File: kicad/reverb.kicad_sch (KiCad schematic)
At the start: 17 parts, among them IC1 TL072CP

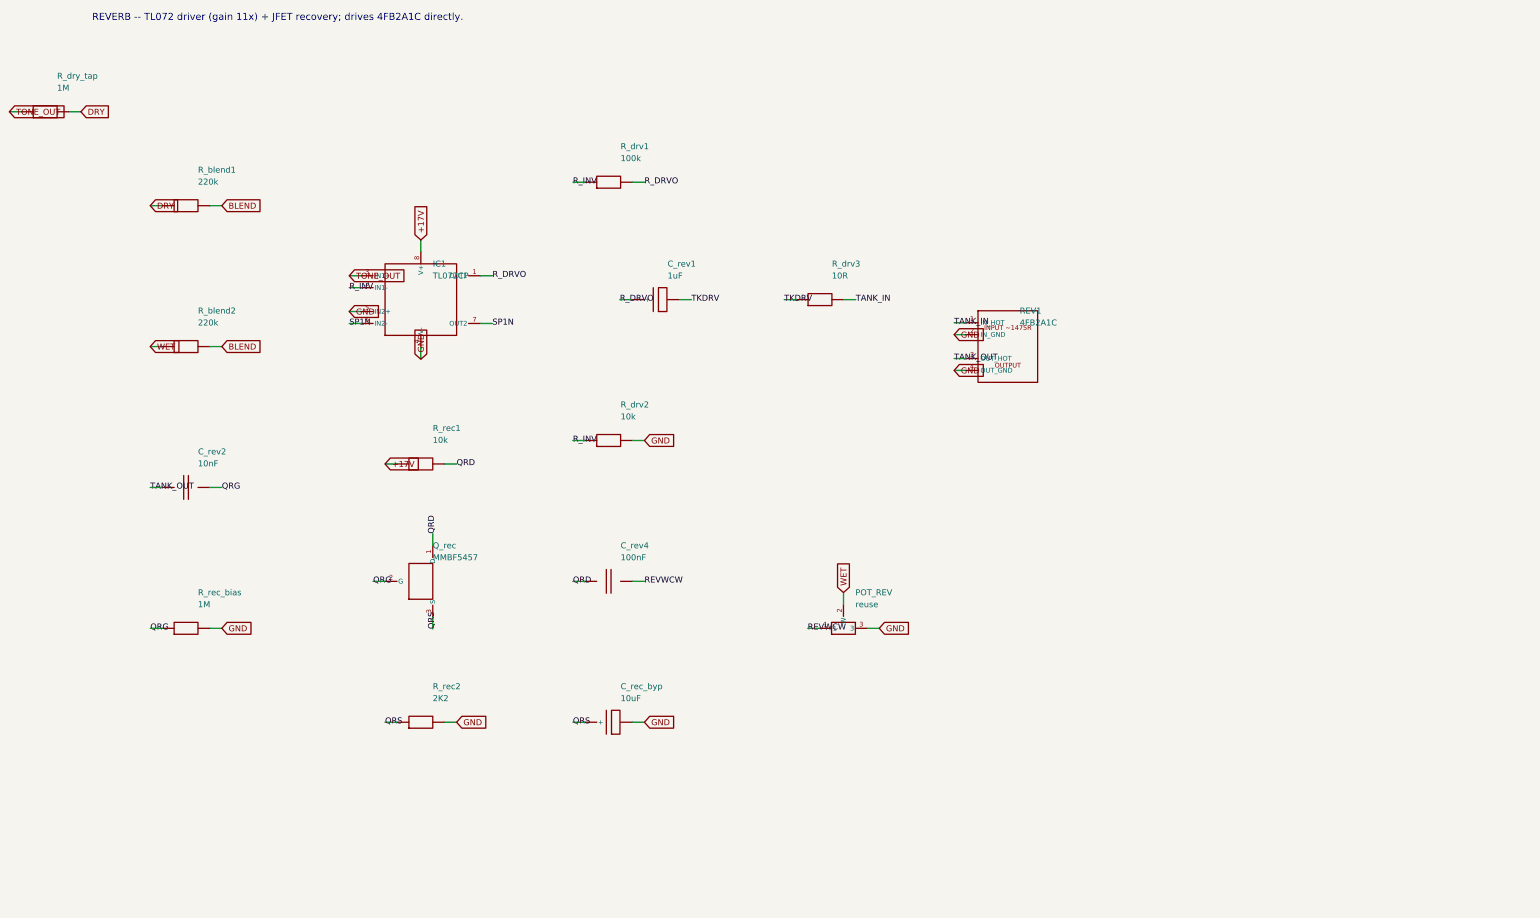
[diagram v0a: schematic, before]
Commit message: Schematic passes KiCad 8 ERC (0 violations); add op-amp mid-rail bias
Installed KiCad 8.0.9 and ran a real Electrical Rules Check on the generated
hierarchy. Drove it to 0 violations:
- snapped every pin/wire endpoint to the 1.27 mm connection grid (was 338
  endpoint_off_grid violations)
- gave the footswitch lines FS_REV/FS_TREM/FS_MRB a real second endpoint via
  100k control pulldowns on the reverb/tremolo/mrb sheets (was 3 dangling labels)

Also made the single-supply TL072 stages electrically real: added a mid-rail
VBIAS network (R_vb1/R_vb2 + C_vb on the Power Supply sheet) and referenced the
reverb driver and tremolo LFO inputs/gain-returns to VBIAS instead of GND
(design addition, flagged in the sheet notes).

Result: kicad-cli 8.0.9 sch erc -> 0 violations; netlist 102 components, 58
nets, 0 unconnected pins; VBIAS spans 10 nodes. Updated SCHEMATIC-BUILD.md,
kicad/README.md, CHANGELOG.md.

https://claude.ai/code/session_01PkrfUi9tvZfLvudJ7h23qD
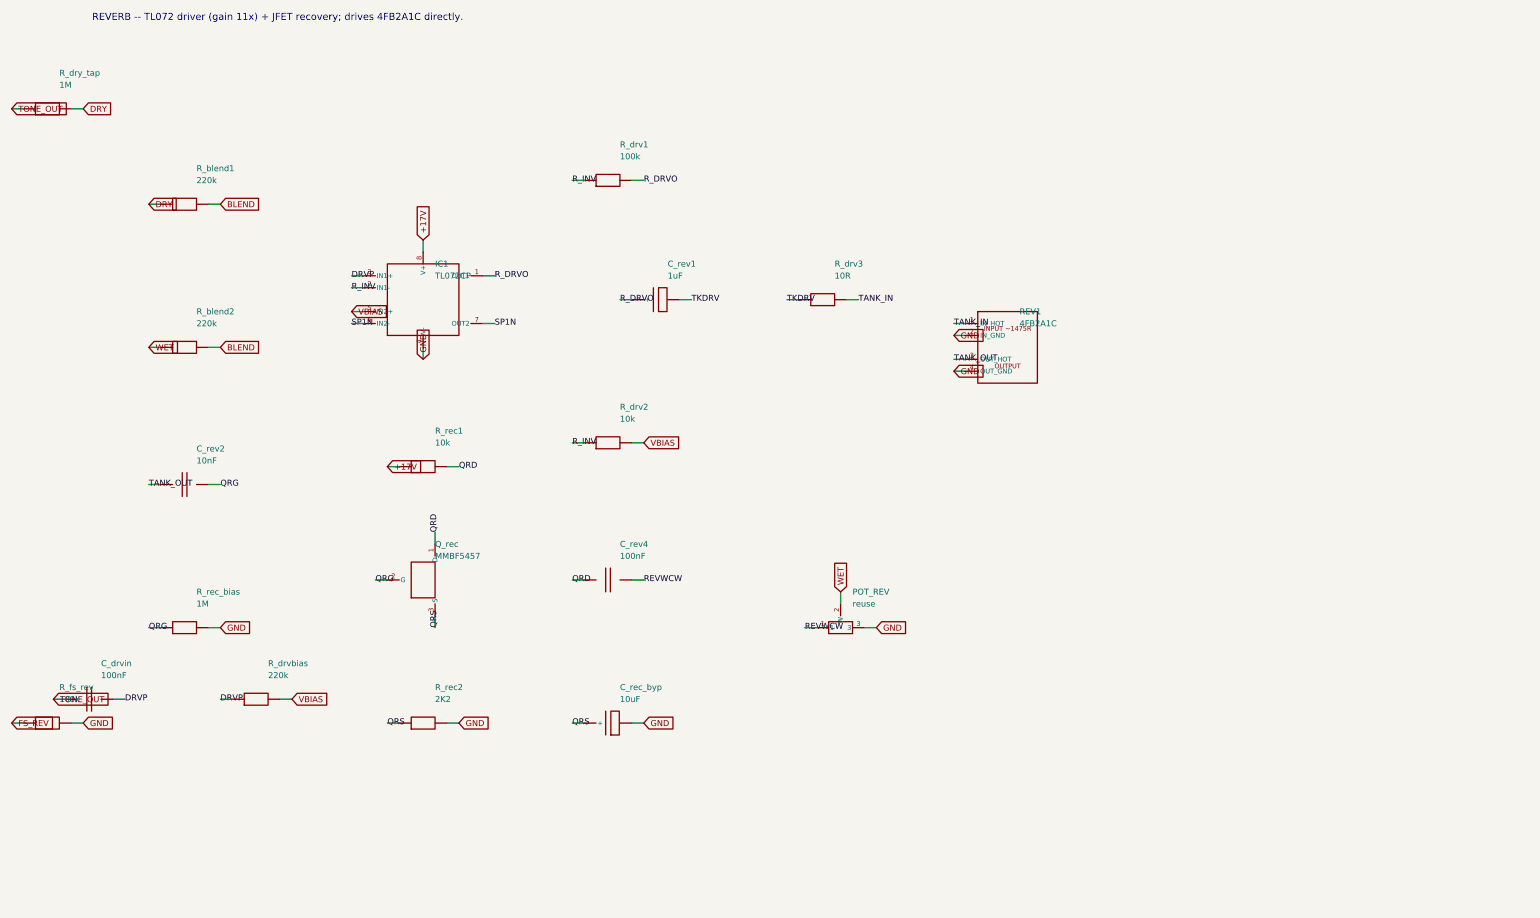
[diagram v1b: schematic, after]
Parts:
- added C_drvin: 100nF, symbol cr_primitives:C
- added R_drvbias: 220k, symbol cr_primitives:R
- added R_fs_rev: 100k, symbol cr_primitives:R
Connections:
- net GND: now also R_fs_rev.2; no longer IC1.5 (IN2+), R_drv2.2
- net TONE_OUT: now also C_drvin.1; no longer IC1.3 (IN1+)
- new net DRVP: C_drvin.2, IC1.3 (IN1+), R_drvbias.1
- new net FS_REV: R_fs_rev.1
- new net VBIAS: IC1.5 (IN2+), R_drv2.2, R_drvbias.2

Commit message: Generate auto-placed PCB (102 footprints, GND pour, board outline)
Build cambridge_reverb.kicad_pcb from the schematic via kicad/gen/gen_pcb.py
(KiCad 8 pcbnew API): assign a THT footprint to every component (standard libs
for generics + the project footprints for VTL5C1 and the 1H toroid), place all
102 footprints (off-board connectors on a bottom wiring-edge strip, toroid in a
reserved spot), assign all 58 nets to pads, draw a 190x115 mm Edge.Cuts outline,
and pour a bottom-layer GND plane. Footprint assignments also carry into the
schematic symbols.

The board opens in KiCad and the ratsnest matches the ERC-clean schematic. It is
placed but NOT routed: kicad-cli pcb drc is dominated by 130 unconnected
(unrouted signal nets; GND is poured) plus cosmetic silk/courtyard overlaps from
dense auto-placement at chassis size -- documented in kicad/PCB-NOTES.md with the
remaining hand-work (placement into floor-plan zones, routing, DRC-to-zero,
Gerbers). Net classes (Default/Power/HighCurrent) carry over for routing.

Also: schematic resistor footprint switched to the compact vertical variant;
gitignore DRC/ERC .rpt reports.

https://claude.ai/code/session_01PkrfUi9tvZfLvudJ7h23qD
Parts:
- C_drvin, C_rev2, C_rev4: footprint (none) -> Capacitor_THT:C_Disc_D7.5mm_W2.5mm_P5.00mm
- C_rec_byp, C_rev1: footprint (none) -> Capacitor_THT:CP_Radial_D8.0mm_P3.50mm
- IC1: footprint (none) -> Package_DIP:DIP-8_W7.62mm
- POT_REV: footprint (none) -> Potentiometer_THT:Potentiometer_Alpha_RD901F-40-00D_Single_Vertical
- Q_rec: footprint (none) -> Package_TO_SOT_THT:TO-92_Inline
- REV1: footprint (none) -> Connector_PinHeader_2.54mm:PinHeader_1x04_P2.54mm_Vertical
- R_blend1, R_blend2, R_drv1, R_drv2, R_drv3, R_drvbias, R_dry_tap, R_fs_rev, R_rec1, R_rec2, R_rec_bias: footprint (none) -> Resistor_THT:R_Axial_DIN0207_L6.3mm_D2.5mm_P5.08mm_Vertical

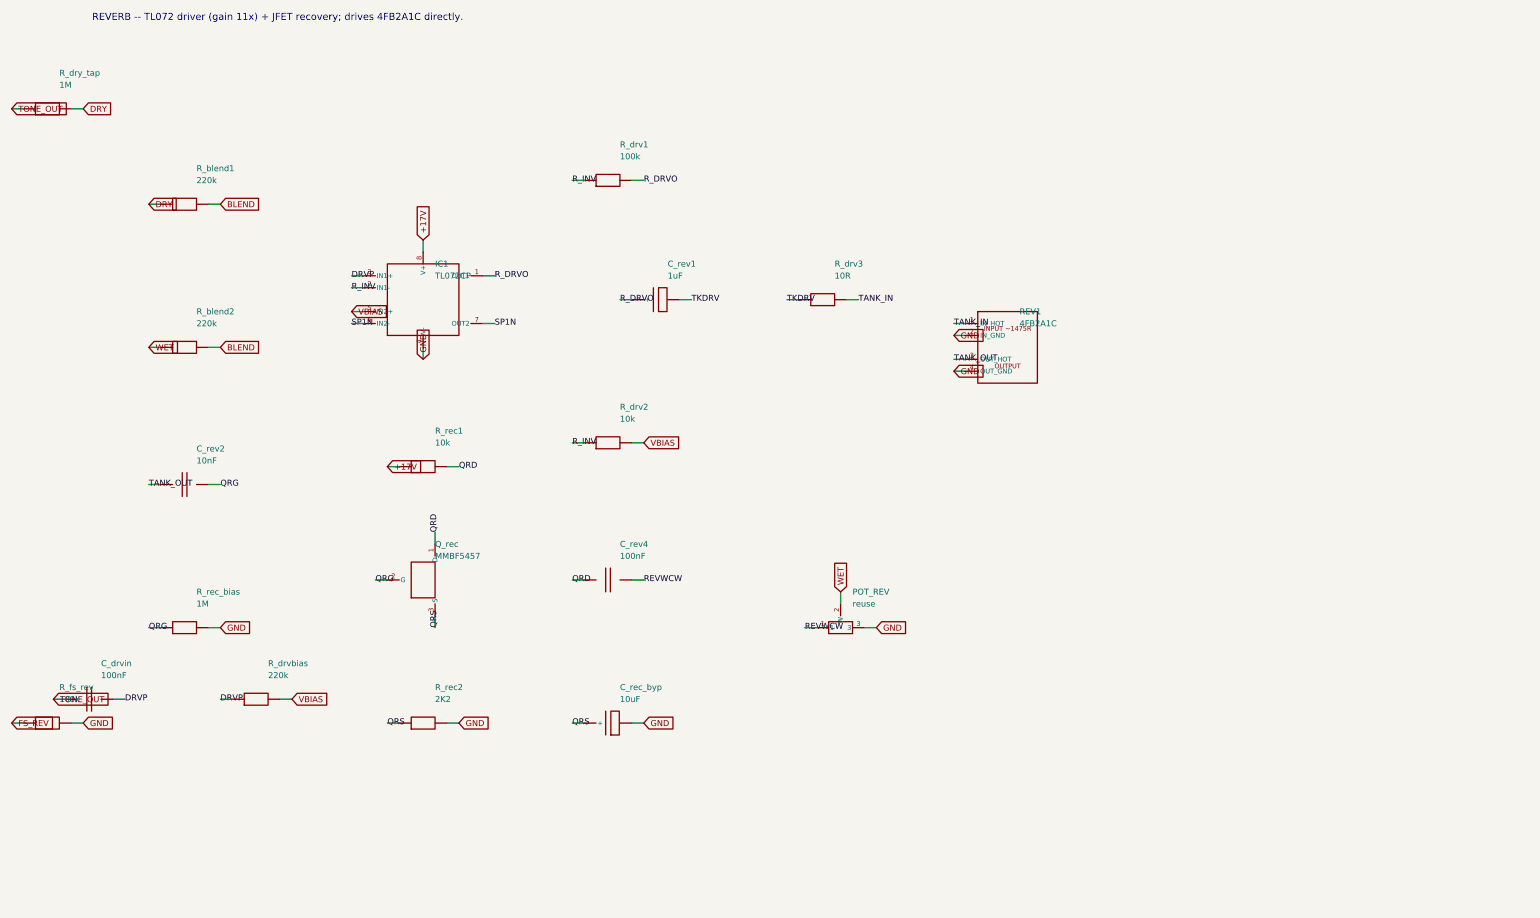
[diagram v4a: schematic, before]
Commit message: Audit pass: center schematic pages, PCB layout audit, SPICE audit
Schematic: gen_kicad.py now defers draw-op emission, computes each sheet's
content bounding box, and translates it to the page center (grid-snapped so pins
stay on the 1.27mm grid). All 8 sheets are centered on the page instead of
crammed top-left; ERC still 0 violations.

PCB: full category-by-category audit in kicad/PCB-AUDIT.md (footprints,
placement, net classes, copper/GND, routing) with prioritized fixes. Applied:
- the 5 reused/off-board pots were modeled with a 16mm panel-pot footprint; they
  are panel-mounted (wired off-board), so they're now 3-pad wiring connectors --
  more correct and a big silk-overlap source removed (packing 51%->48%)
- centered the component grid
Documented findings: LM1875 TO-220-5 annular is 0.0875mm (1.275mm pad on 1.1mm
drill) vs the 0.15mm rule; KBP410G bridge uses a placeholder header footprint;
silk/courtyard overlaps are a density symptom (the 82% packing on the 155x90
safe-bet). Non-routing DRC errors: 9; demo board still 0.

SPICE: audited every netlist/model (spice/README.md). All five run under
ngspice-42 (exit 0) and match the documented numbers; no correctness issues.

https://claude.ai/code/session_01PkrfUi9tvZfLvudJ7h23qD
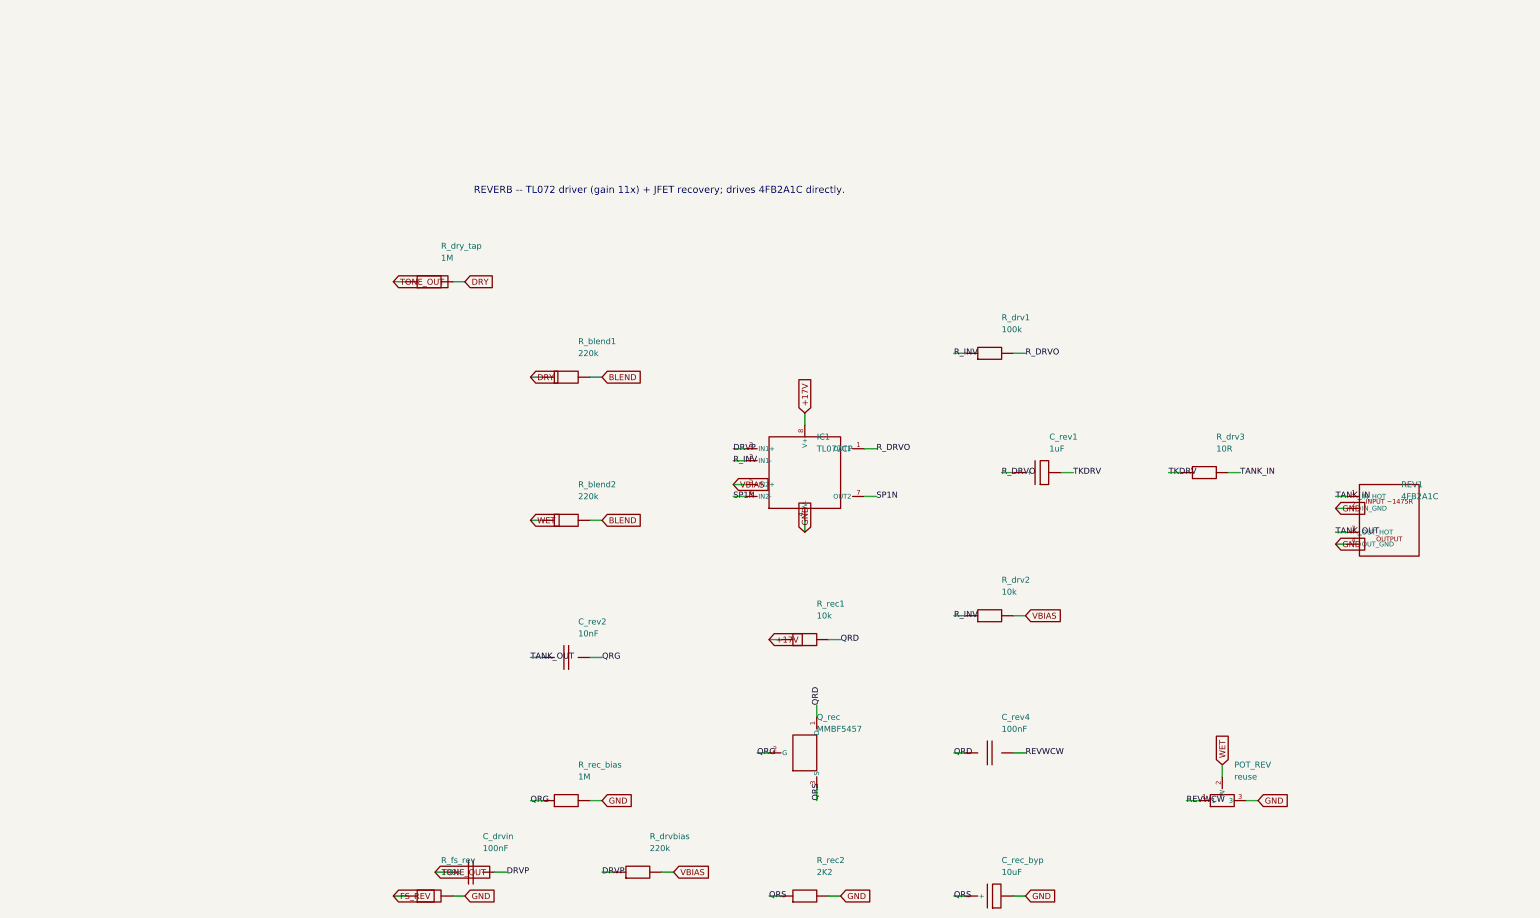
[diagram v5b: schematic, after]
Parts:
- POT_REV: footprint Potentiometer_THT:Potentiometer_Alpha_RD901F-40-00D_Single_Vertical -> Connector_PinHeader_2.54mm:PinHeader_1x03_P2.54mm_Vertical
